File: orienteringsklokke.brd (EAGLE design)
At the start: 50 x 50 mm, 15 parts

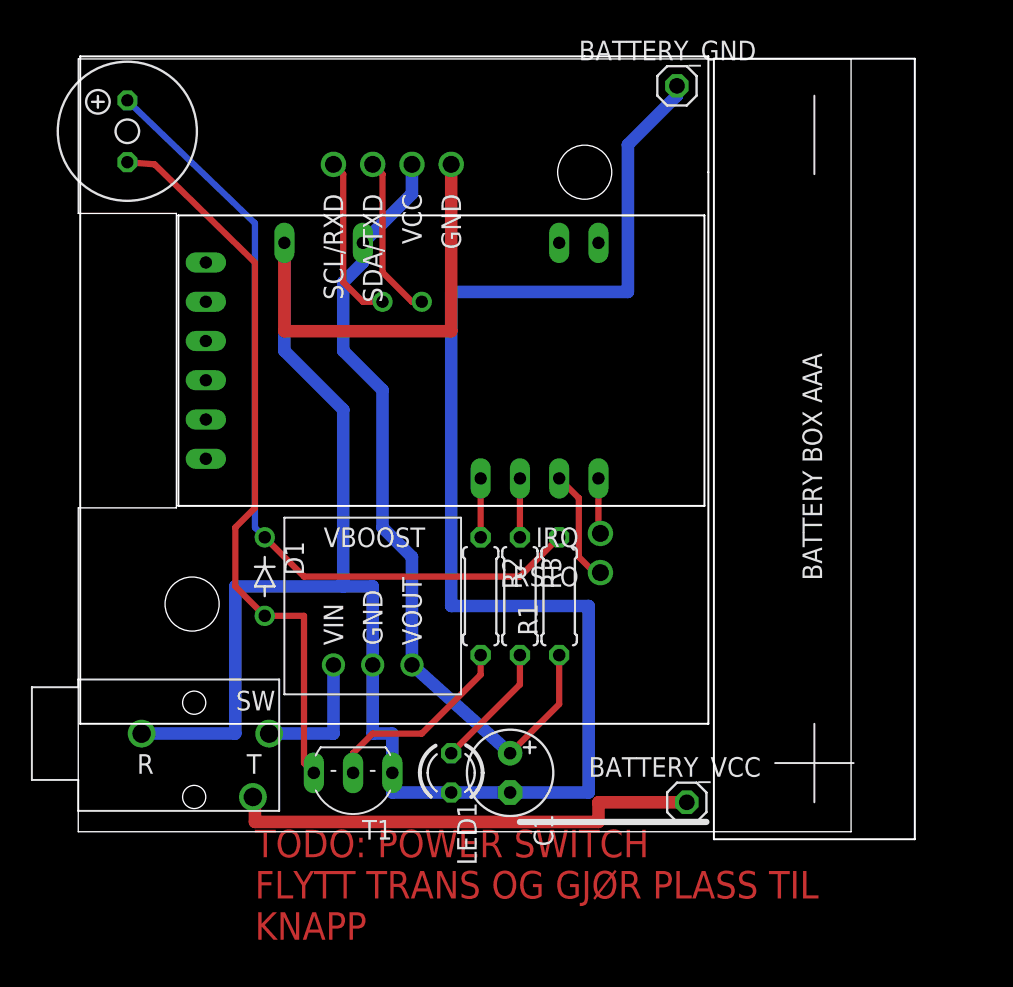
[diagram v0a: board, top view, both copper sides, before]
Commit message: Fully traced with jack, switch, buzzer and no battery box
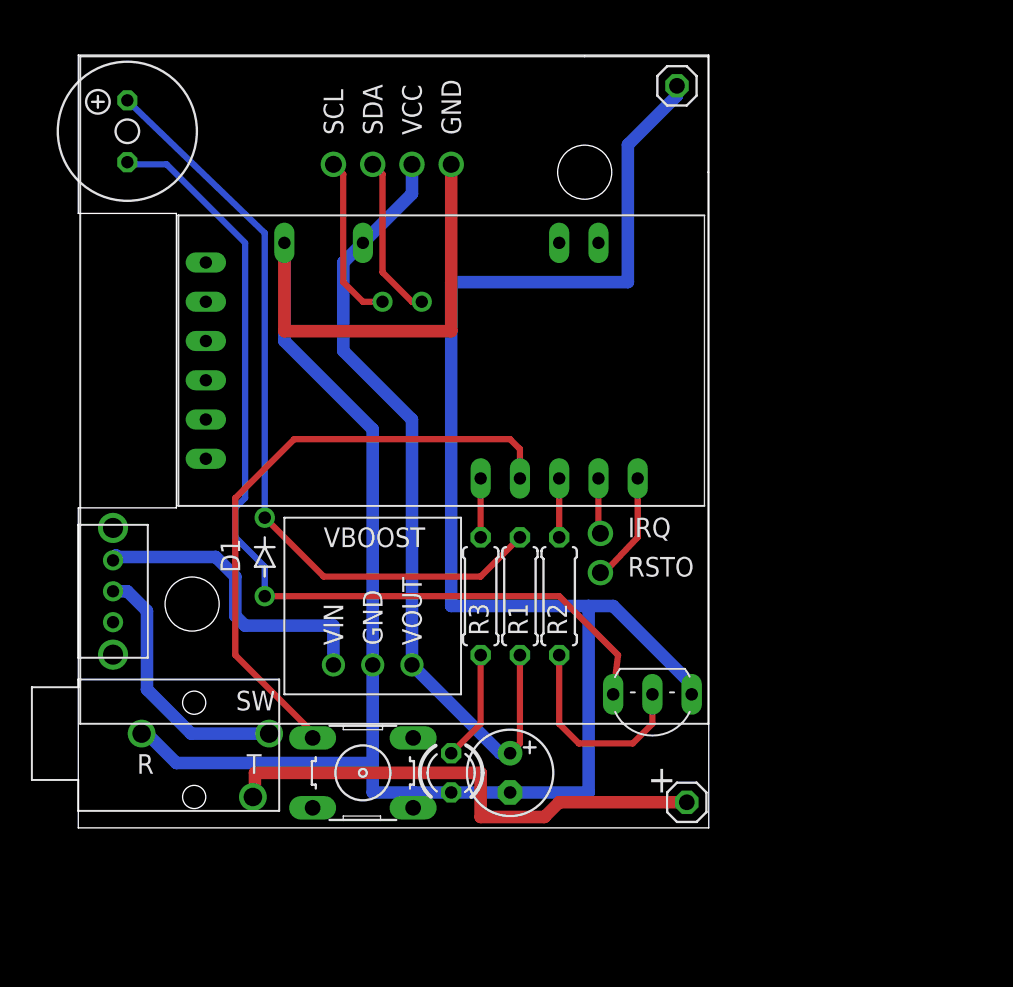
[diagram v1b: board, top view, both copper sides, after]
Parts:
- removed U$5: BATTERY-BOX, joakim:AAA-BATTERY-BOX-SINGLE
- added S1: (no value), switch-omron:B3F-10XX
- added U$6: SK12D07-SLIDE-SWITCH, joakim:SK12D07
- moved T1 20.0 mm to (37.1, 7.62)
- moved R2 5.08 mm to (31.1, 15.2)
- moved R1 2.54 mm to (28.6, 15.2)
- moved R3 2.54 mm to (26.0, 15.2)
- moved D1 1.27 mm to (12.1, 17.8)
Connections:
- new net N$1: CHARGE.SWITCH, U$6.2
- new net SWITCH: S1.1, U$4.D5
- net BUZZER: now also U$4.D6; no longer U$4.D4
- net GND: now also S1.4
- net LED: now also U$4.D4; no longer U$4.D5
- net N$7: now also U$6.3; no longer CHARGE.SWITCH
- net RSTO: now also U$4.D8; no longer U$4.D6
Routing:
- net SWITCH: track 0.00 -> 39.8 mm
- net N$1: track 0.00 -> 16.9 mm
- net N$2: track 48.0 -> 60.7 mm
- net N$7: track 8.61 -> 20.3 mm
- net N$4: track 53.2 -> 49.9 mm
- net N$6: track 31.4 -> 34.0 mm
- net GND: track 170.2 -> 172.7 mm
- net N$5: track 8.19 -> 7.14 mm
- net +3V3: track 52.3 -> 51.4 mm
- net N$3: track 12.9 -> 13.4 mm
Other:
- board size 50 x 50 mm -> 40.8 x 50 mm
- board text added: "+"
- board text removed: "TODO: POWER SWITCH FLYTT TRANS OG GJØR PLASS TIL KNAPP"
